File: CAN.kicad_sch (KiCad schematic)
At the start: 10 parts, among them J5 Conn_01x02_Pin, U5 TCAN337, U6 CDSOT23-T24CAN

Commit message: finished? power on sch
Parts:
- renumbered C19 to C6, C20 to C9, D15 to D1, JP3 to JP1, R26 to R10, R22 to R13, R25 to R5, U5 to U4, U6 to U5
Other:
- moved on the sheet: C6, C9, D1, J5, JP1, R10, R13, R5, U4, U5

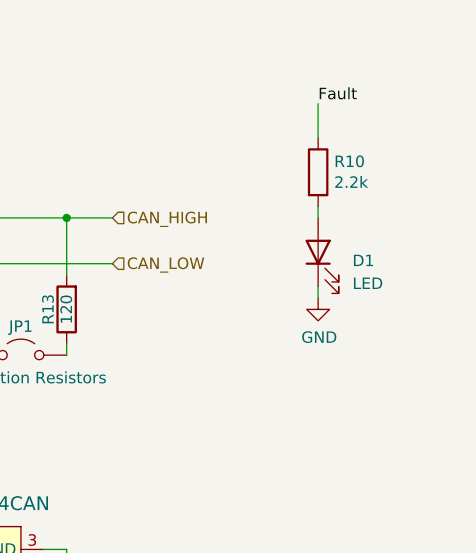
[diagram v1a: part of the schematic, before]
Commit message: added MX cube pinout screenshot
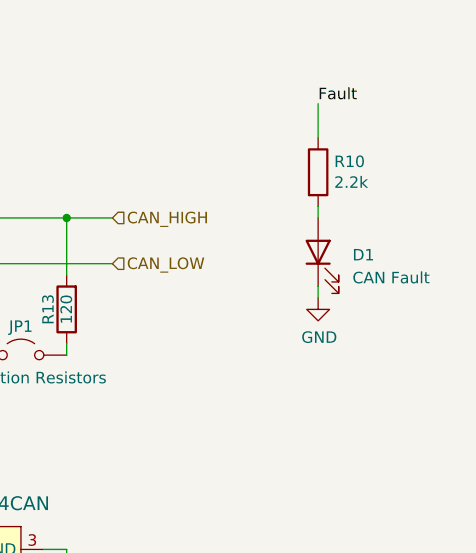
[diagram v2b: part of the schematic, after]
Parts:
- D1: value LED -> CAN Fault
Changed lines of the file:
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@@
 		(fields_autoplaced yes)
 		(property "Reference" "D1"
-			(at 171.45 80.9625 90)
+			(at 171.45 80.3274 90)
 			(effects
 				(font
@@
 			)
 		)
-		(property "Value" "LED"
-			(at 171.45 83.5025 90)
+		(property "Value" "CAN Fault"
+			(at 171.45 82.8674 90)
 			(effects
 				(font

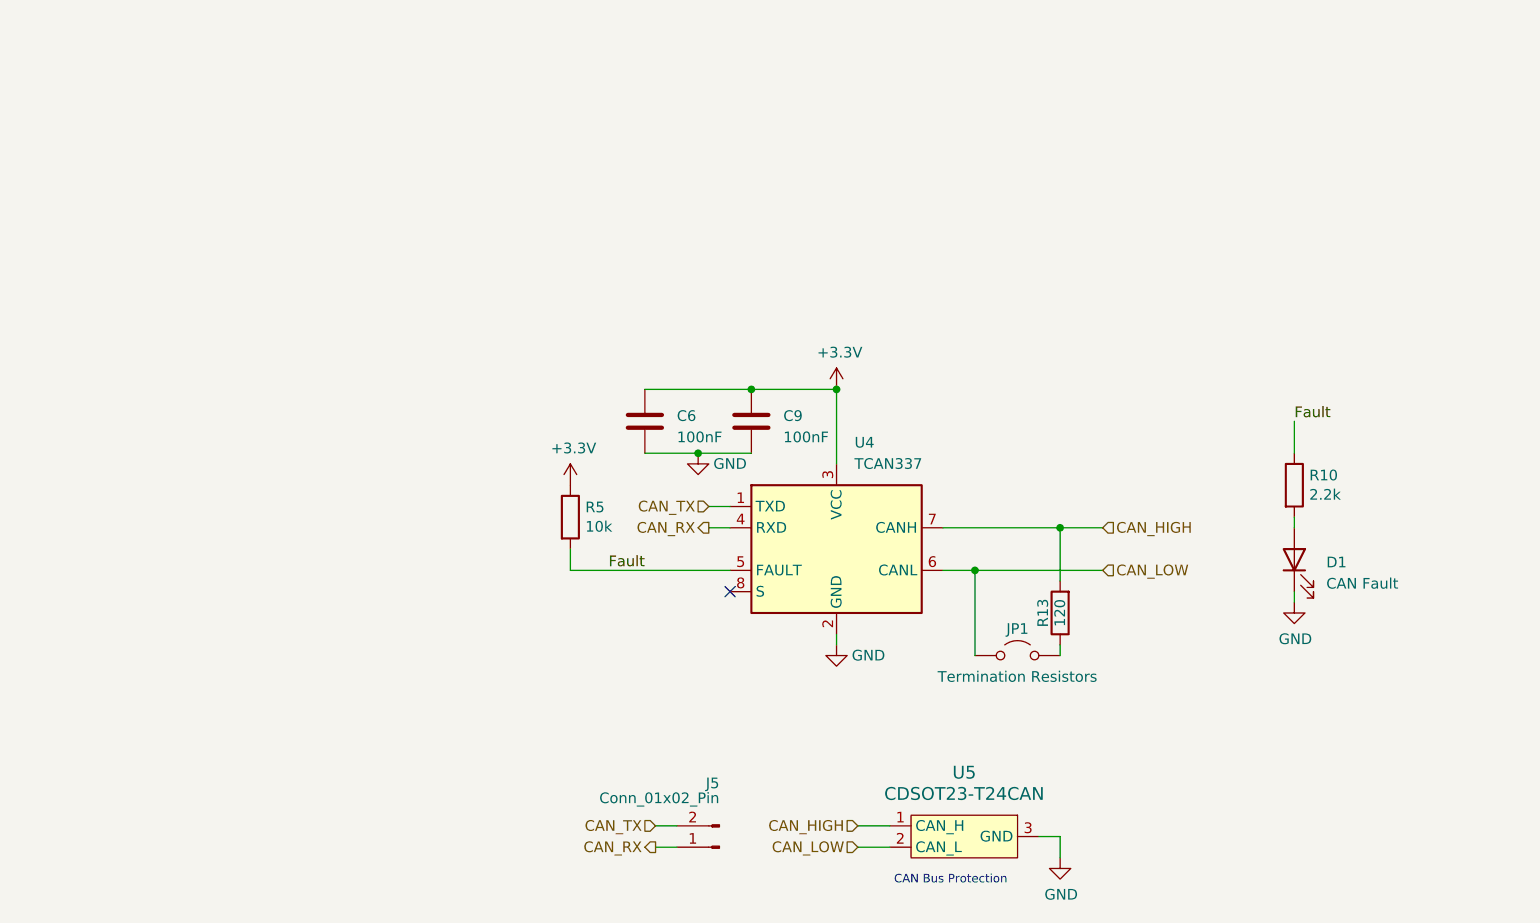
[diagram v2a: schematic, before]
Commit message: added 24V buck, bypass caps, more LEDs; started scrutineering circuit and bidirectional current sense
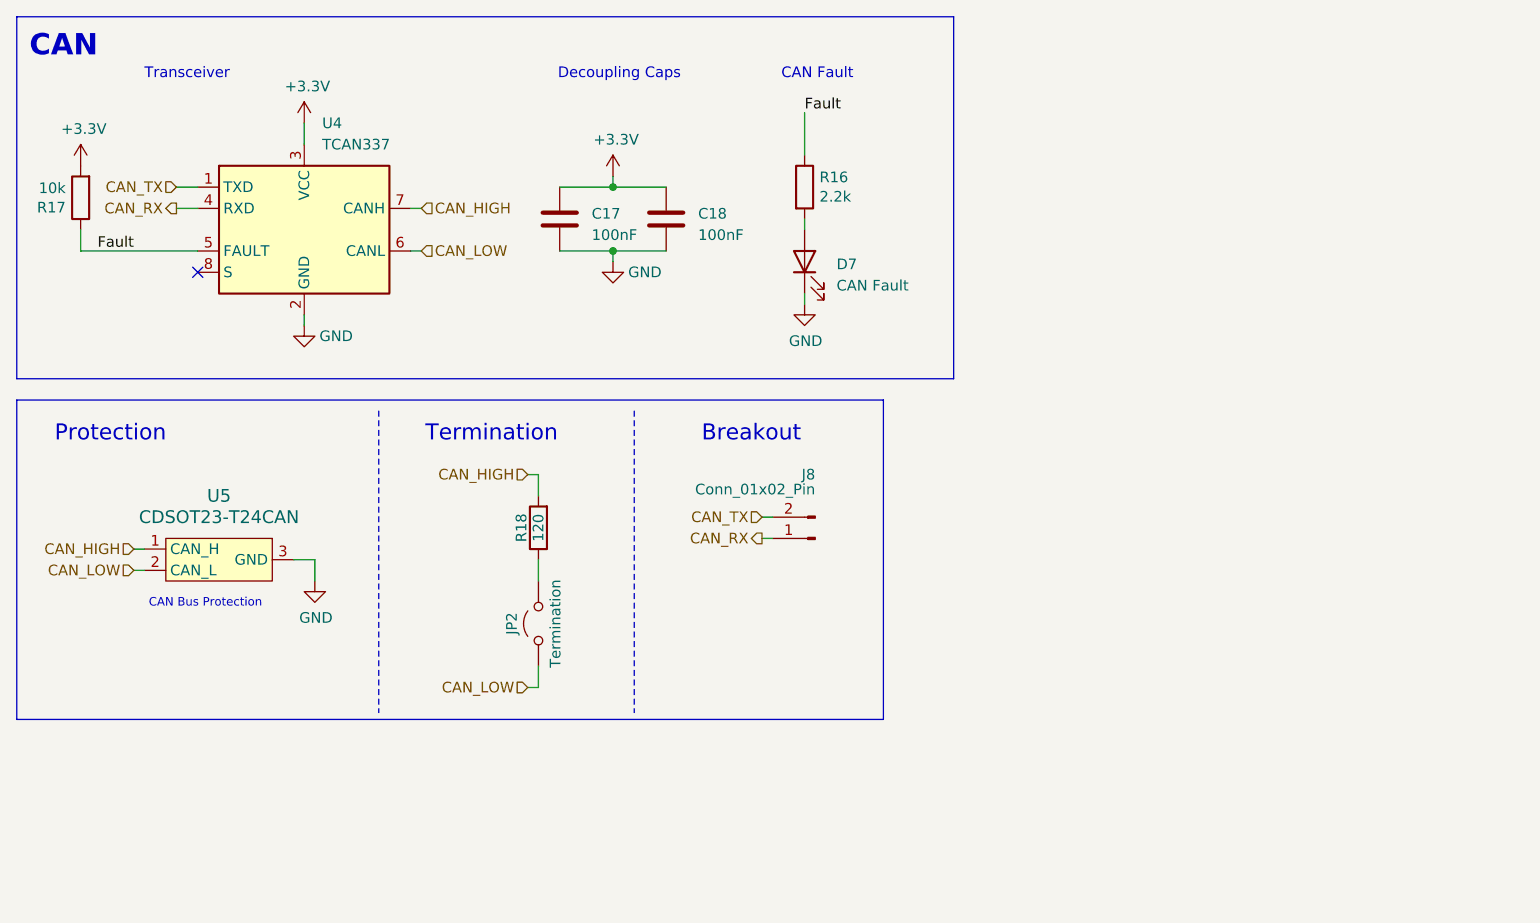
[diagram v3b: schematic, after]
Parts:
- JP2: renamed from JP1; value Termination Resistors -> Termination
- renumbered C6 to C17, C9 to C18, D1 to D7, J5 to J8, R10 to R16, R5 to R17, R13 to R18
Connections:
- net +3.3V: now also R17.2; no longer R17.1
- net Fault: now also R17.1; no longer R17.2
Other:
- note added: "Breakout"
- note added: "CAN"
- note added: "CAN Fault"
- note added: "Decoupling Caps"
- note added: "Protection"
- note added: "Termination"
- note added: "Transceiver"
- moved on the sheet: C17, C18, D7, J8, JP2, R16, R17, R18, U4, U5
